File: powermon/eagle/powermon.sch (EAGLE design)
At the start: 25 parts, among them J1 USBSMD, J3 USBSMD, U1 LTC2290, U2 FT232RL, U3 ATMEGA328, X1 16MHz

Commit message: Updated schematic.
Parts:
- removed JP2: (no value), powermon:PINHD-1X2
- added C1, C4: 10uF, powermon:CPOL-USA/3216-18R
- added C5, C8, C9: 0.1uF, powermon:C-USC0805
- added J2: TERMINAL-2, powermon:TERMINAL-2
- added JP1: (no value), powermon:PINHD-1X9
- added R10: (no value), powermon:SHUNT
- added R11: 3.3K, powermon:R-US_R0805
- added R2: 8k 1%, powermon:R-US_R0805
- added R3: 3.3K 1%, powermon:R-US_R0805
- added R99: 1K, powermon:TRIM_US-SM-42/43A
- added S1: 219-04, powermon:219-04
- added U4: LTE1764, powermon:LTE1764
- U1: value LTC2290 -> INA219; device powermon:LTC2290 -> powermon:INA219
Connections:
- new net CONFIG1: S1.8, U3.PC3(ADC3)
- new net CONFIG2: S1.7, U3.PC2(ADC2)
- new net CONFIG3: S1.6, U3.PC1(ADC1)
- new net CONFIG4: S1.5, U3.PC0(ADC0)
- new net I2C-CLK: R11.1, U1.SCL, U3.PC5(ADC5/SCL)
- new net I2C-DATA: R1.1, U1.SDA, U3.PC4(ADC4/SDA)
- new net N$18: R3.1, R99.E, R99.S
- new net N$19: R2.2, R99.A, U4.ADJ
- new net N$5: J2.2, R10.I1, R2.1
- new net N$9: C4.+, C5.1, J1.VBUS, U4.IN, U4.SHDN
- new net SENSE+: R10.V2, U1.VIN+
- new net SENSE-: R10.V1, U1.VIN-
- new net V+: C1.+, C8.1, R10.I2, U4.OUT
- net +5V: now also C9.1, R1.2, R11.2
- net GND: now also C1.-, C4.-, C5.2, C8.2, C9.2, J1.GND, J2.1, R3.2, S1.1, S1.2, S1.3, S1.4, U4.GND@1, U4.GND@2
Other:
- note added: "FROM CHARGER"
- note added: "LOGIC ANALYZER"
- note added: "SETTINGS"
- note added: "TO COMPUTER"
- note added: "TO DEVICE"
- note added: "V/A SENSE"
- note added: "VOLTAGE REGULATOR"
- note removed: "POWER"
- note removed: "SENSE"
- moved on the sheet: C10, C2, C3, C6, C7, J1, J3, J5, R1, R4, U2, U3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

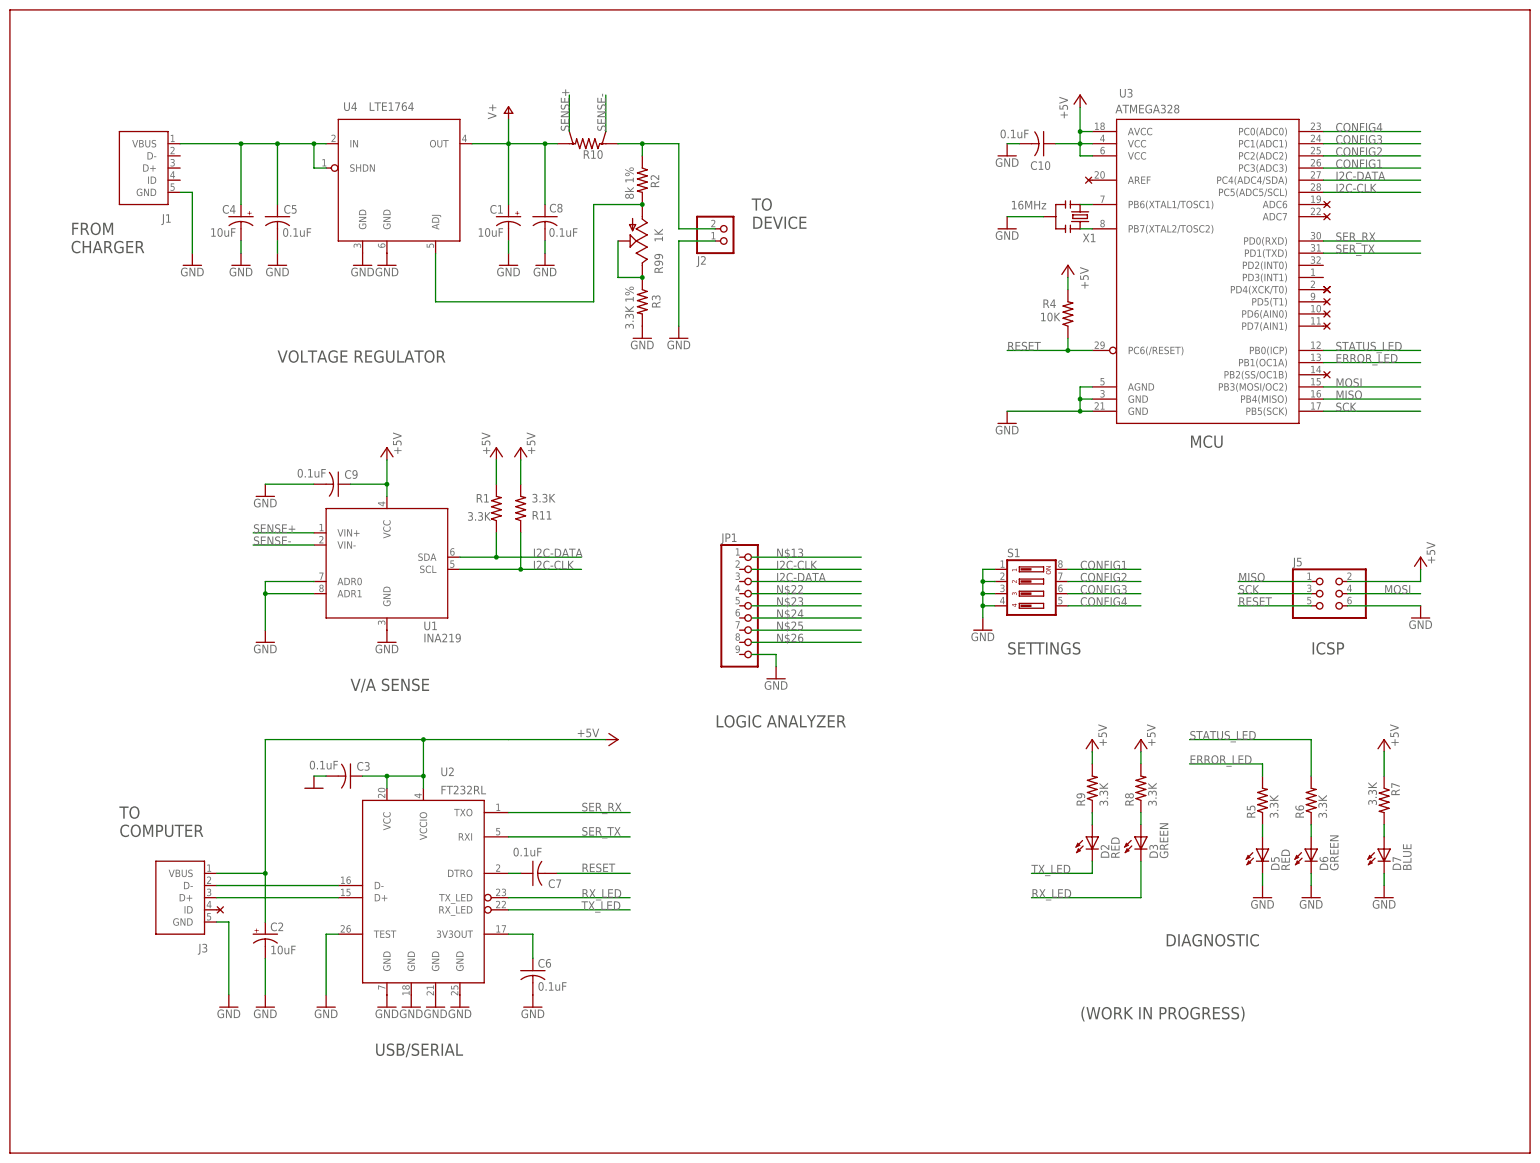
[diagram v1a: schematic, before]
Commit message: More progress with the powermon schematic. Incomplete.
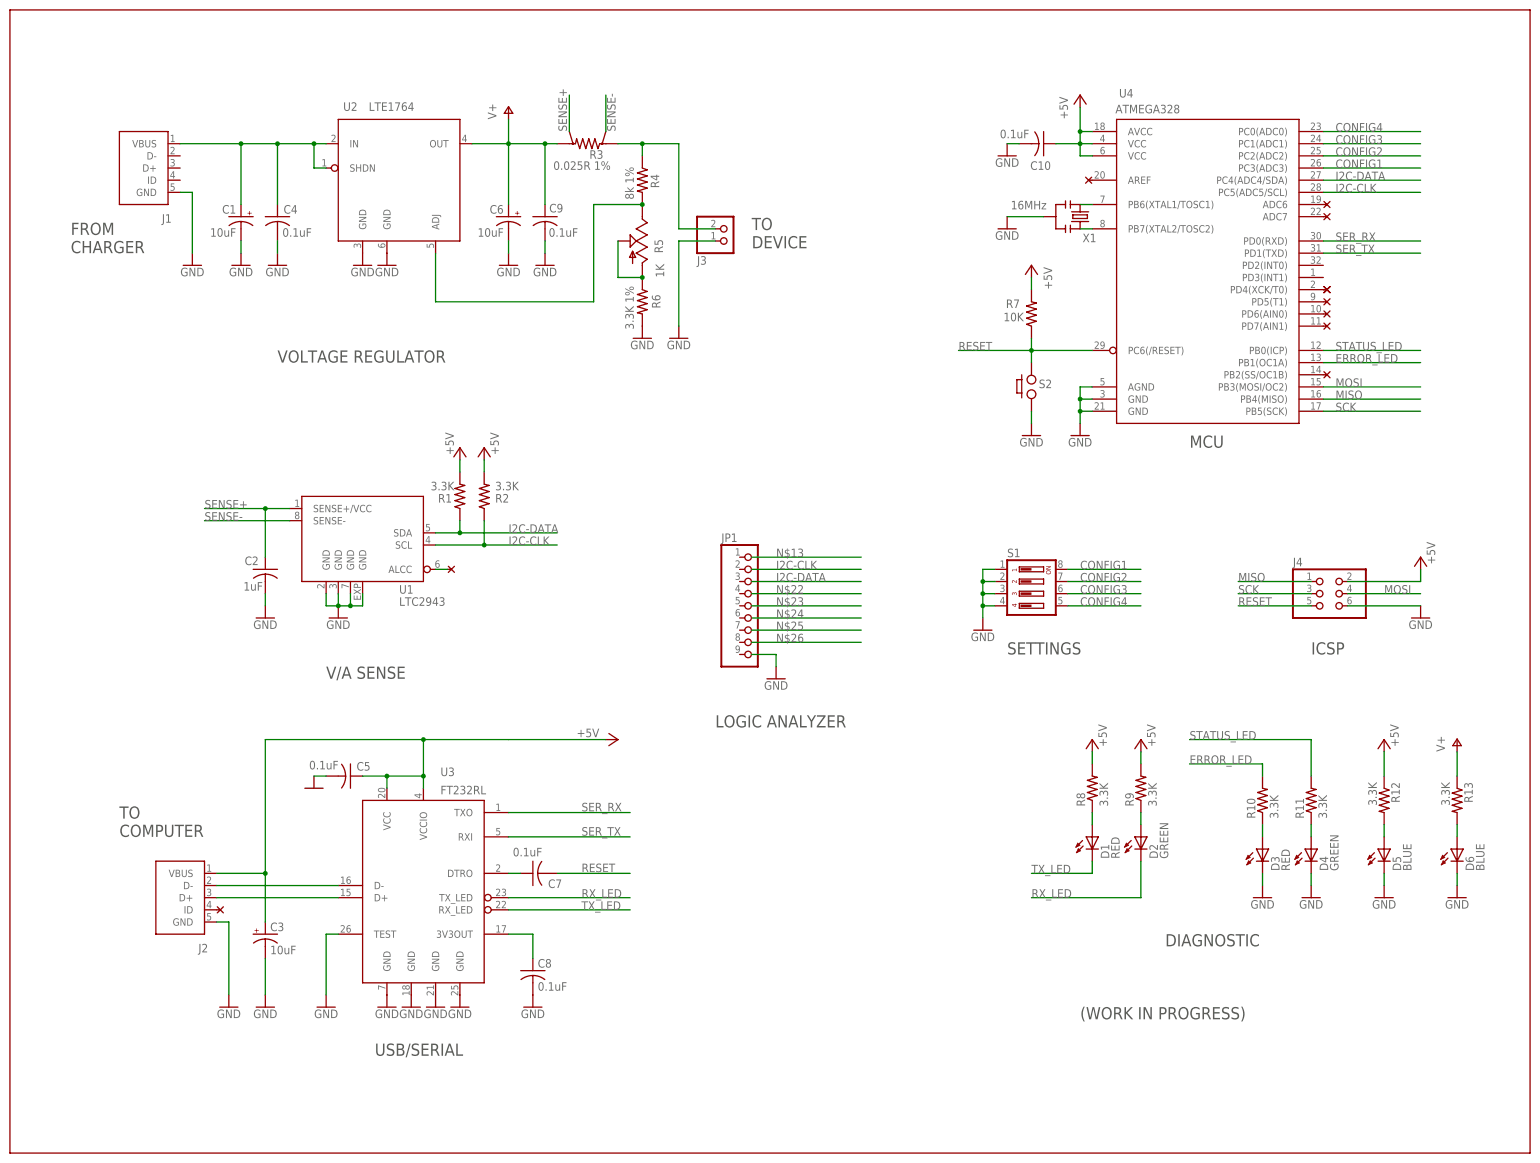
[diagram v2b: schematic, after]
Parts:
- removed D7: BLUE, powermon:LED
- removed R99: 1K, powermon:TRIM_US-SM-42/43A
- added D1: RED, powermon:LED
- added D4: GREEN, powermon:LED
- added R12, R13: 3.3K, powermon:R-US_R0805
- added S2: PUSH_BUTTON, powermon:PUSH_BUTTON
- C2: value 10uF -> 1uF; device powermon:CPOL-USA/3216-18R -> powermon:C-USC0805
- C3: value 0.1uF -> 10uF; device powermon:C-USC0805 -> powermon:CPOL-USA/3216-18R
- C4: value 10uF -> 0.1uF; device powermon:CPOL-USA/3216-18R -> powermon:C-USC0805
- C6: value 0.1uF -> 10uF; device analyzer:C-USC0805 -> powermon:CPOL-USA/3216-18R
- C8: device powermon:C-USC0805 -> analyzer:C-USC0805
- D2: value RED -> GREEN
- D3: value GREEN -> RED
- D5: value RED -> BLUE
- D6: value GREEN -> BLUE
- J2: value TERMINAL-2 -> USBSMD; device powermon:TERMINAL-2 -> powermon:USBSMD
- J3: value USBSMD -> TERMINAL-2; device powermon:USBSMD -> powermon:TERMINAL-2
- R10: value (none) -> 3.3K; device powermon:SHUNT -> powermon:R-US_R0805
- R2: value 8k 1% -> 3.3K
- R3: value 3.3K 1% -> 0.025R 1%; device powermon:R-US_R0805 -> powermon:SHUNT
- R4: value 10K -> 8k 1%
- R5: value 3.3K -> 1K; device powermon:R-US_R0805 -> powermon:TRIM_US-SM-42/43A
- R6: value 3.3K -> 3.3K 1%
- R7: value 3.3K -> 10K
- U1: value INA219 -> LTC2943; device powermon:INA219 -> powermon:LTC2943SMD
- U2: value FT232RL -> LTE1764; device powermon:FT232RL -> powermon:LTE1764
- U3: value ATMEGA328 -> FT232RL; device powermon:ATMEGA328 -> powermon:FT232RL
- U4: value LTE1764 -> ATMEGA328; device powermon:LTE1764 -> powermon:ATMEGA328
- renumbered J5 to J4
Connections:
- removed net N$8 (its old number): D3.A, R8.1
- new net GND@3: U1.GND@2, U1.GND@3, U1.GND@7, U1.GND@9
- new net N$1: U1.ALCC
- new net N$14: D6.A, R13.2
- new net N$6: D1.A, R8.1
- net +5V: now also R12.1, R2.2, R7.2, U4.AVCC, U4.VCC@1, U4.VCC@2; no longer C9.1, R11.2, R4.2, R7.1, U1.VCC, U3.AVCC, U3.VCC@1, U3.VCC@2
- net CONFIG1: now also U4.PC3(ADC3); no longer U3.PC3(ADC3)
- net CONFIG2: now also U4.PC2(ADC2); no longer U3.PC2(ADC2)
- net CONFIG3: now also U4.PC1(ADC1); no longer U3.PC1(ADC1)
- net CONFIG4: now also U4.PC0(ADC0); no longer U3.PC0(ADC0)
- net ERROR_LED: now also R10.2, U4.PB1(OC1A); no longer R5.2, U3.PB1(OC1A)
- net GND: now also C2.2, C3.-, C4.2, C6.-, D3.C, D4.C, J2.GND, J3.1, R6.2, S2.P$4, U3.GND@3, U3.GND@4, U3.TEST, U4.AGND; no longer C2.-, C3.2, C4.-, C6.2, D7.C, J2.1, J3.GND, R3.2, U1.ADR0, U1.ADR1, U1.GND, U2.GND@3, U2.GND@4, U2.TEST, U3.AGND
- net I2C-CLK: now also R2.1, U4.PC5(ADC5/SCL); no longer R11.1, U3.PC5(ADC5/SCL)
- net I2C-DATA: now also U4.PC4(ADC4/SDA); no longer U3.PC4(ADC4/SDA)
- net MISO: now also U4.PB4(MISO); no longer U3.PB4(MISO)
- net MOSI: now also U4.PB3(MOSI/OC2); no longer U3.PB3(MOSI/OC2)
- net N$10: now also J2.D+, U3.D+; no longer J3.D+, U2.D+
- net N$11: now also U3.DTRO; no longer U2.DTRO
- net N$12: now also C3.+, C5.1, J2.VBUS, U3.VCC, U3.VCCIO; no longer C2.+, C3.1, J3.VBUS, U2.VCC, U2.VCCIO
- net N$15: now also J2.D-, U3.D-; no longer J3.D-, U2.D-
- net N$16: now also C8.1, U3.3V3OUT; no longer C6.1, U2.3V3OUT
- net N$17: now also D5.A, R12.2; no longer D7.A, R7.2
- net N$18: now also R5.A, R5.S, R6.1; no longer R3.1, R99.E, R99.S
- net N$19: now also R4.2, R5.E, U2.ADJ; no longer R2.2, R99.A, U4.ADJ
- net N$2: now also U4.PB7(XTAL2/TOSC2); no longer U3.PB7(XTAL2/TOSC2)
- net N$3: now also D4.A, R11.1; no longer D6.A, R6.1
- net N$4: now also D3.A, R10.1; no longer D5.A, R5.1
- net N$5: now also J3.2, R3.I1, R4.1; no longer J2.2, R10.I1, R2.1
- net N$7: now also U4.PB6(XTAL1/TOSC1); no longer U3.PB6(XTAL1/TOSC1)
- net N$9: now also C1.+, C4.1, U2.IN, U2.SHDN; no longer C4.+, C5.1, U4.IN, U4.SHDN
- net RESET: now also R7.1, S2.P$3, U4.PC6(/RESET); no longer R4.1, U3.PC6(/RESET)
- net RX_LED: now also D2.C, U3.TX_LED; no longer D3.C, U2.TX_LED
- net SCK: now also U4.PB5(SCK); no longer U3.PB5(SCK)
- net SENSE+: now also C2.1, R3.V2, U1.SENSE+/VCC; no longer R10.V2, U1.VIN+
- net SENSE-: now also R3.V1, U1.SENSE-; no longer R10.V1, U1.VIN-
- net SER_RX: now also U3.TXO, U4.PD0(RXD); no longer U2.TXO, U3.PD0(RXD)
- net SER_TX: now also U3.RXI, U4.PD1(TXD); no longer U2.RXI, U3.PD1(TXD)
- net STATUS_LED: now also R11.2, U4.PB0(ICP); no longer R6.2, U3.PB0(ICP)
- net TX_LED: now also D1.C, U3.RX_LED; no longer D2.C, U2.RX_LED
- net V+: now also C6.+, C9.1, R13.1, R3.I2, U2.OUT; no longer C1.+, C8.1, R10.I2, U4.OUT
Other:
- moved on the sheet: C1, C5, C8, C9, D2, D3, D5, D6, R1, R11, R2, R4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

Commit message: Updated schematic.
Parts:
- U2: value LTE1764 -> LT1764AEQ
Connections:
- net STATUS_LED renamed ACTIVITY_LED
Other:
- note added: "3.8V"
- moved on the sheet: C1, C4, C6, C9, R7, S2
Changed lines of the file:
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@@
 <part name="P+7" library="powermon" deviceset="+5V" device=""/>
 <part name="GND4" library="powermon" deviceset="GND" device=""/>
-<part name="U2" library="powermon" deviceset="LTE1764" device=""/>
+<part name="U2" library="powermon" deviceset="LTE1764" device="" value="LT1764AEQ"/>
 <part name="GND19" library="powermon" deviceset="GND" device=""/>
 <part name="GND20" library="powermon" deviceset="GND" device=""/>
@@
 <text x="-22.86" y="187.96" size="2.54" layer="97">FROM
 CHARGER</text>
-<text x="111.76" y="88.9" size="2.54" layer="97">LOGIC ANALYZER</text>
+<text x="111.76" y="91.44" size="2.54" layer="97">LOGIC ANALYZER</text>
 <text x="-12.7" y="66.04" size="2.54" layer="97">TO
 COMPUTER</text>
@@
 DEVICE</text>
 <text x="172.72" y="104.14" size="2.54" layer="97">SETTINGS</text>
+<text x="97.028" y="213.106" size="2.54" layer="97">3.8V</text>
 </plain>
 <instances>
@@
 <attribute name="VALUE" x="173.482" y="198.882" size="1.778" layer="96" rot="MR180"/>
 </instance>
-<instance part="GND8" gate="1" x="172.72" y="193.04"/>
+<instance part="GND8" gate="1" x="170.18" y="193.04"/>
 <instance part="D3" gate="G$1" x="226.06" y="63.5"/>
 <instance part="D4" gate="G$1" x="236.22" y="63.5"/>
-<instance part="R7" gate="G$1" x="177.8" y="175.26" smashed="yes" rot="R90">
-<attribute name="NAME" x="172.466" y="176.5046" size="1.778" layer="95"/>
-<attribute name="VALUE" x="171.958" y="173.736" size="1.778" layer="96"/>
-</instance>
-<instance part="P+1" gate="1" x="177.8" y="185.42" rot="MR0"/>
+<instance part="R7" gate="G$1" x="180.34" y="175.26" smashed="yes" rot="R90">
+<attribute name="NAME" x="175.006" y="176.5046" size="1.778" layer="95"/>
+<attribute name="VALUE" x="174.498" y="173.736" size="1.778" layer="96"/>
+</instance>
+<instance part="P+1" gate="1" x="180.34" y="185.42" rot="MR0"/>
 <instance part="C10" gate="G$1" x="180.34" y="210.82" smashed="yes" rot="R270">
 <attribute name="NAME" x="177.546" y="205.359" size="1.778" layer="95"/>
@@
 </instance>
 <instance part="C3" gate="G$1" x="17.78" y="45.72"/>
-<instance part="GND1" gate="1" x="172.72" y="208.28" rot="MR0"/>
+<instance part="GND1" gate="1" x="170.18" y="208.28" rot="MR0"/>
 <instance part="D5" gate="G$1" x="251.46" y="63.5"/>
 <instance part="R12" gate="G$1" x="251.46" y="73.66" rot="R270"/>
@@
 <instance part="GND22" gate="1" x="96.52" y="170.18"/>
 <instance part="GND23" gate="1" x="104.14" y="170.18"/>
-<instance part="C6" gate="G$1" x="68.58" y="195.58" rot="MR0"/>
-<instance part="C1" gate="G$1" x="12.7" y="195.58" rot="MR0"/>
+<instance part="C6" gate="G$1" x="68.58" y="198.12" rot="MR0"/>
+<instance part="C1" gate="G$1" x="12.7" y="198.12" rot="MR0"/>
 <instance part="GND24" gate="1" x="12.7" y="185.42"/>
-<instance part="C4" gate="G$1" x="20.32" y="195.58" smashed="yes">
-<attribute name="NAME" x="21.59" y="196.215" size="1.778" layer="95"/>
-<attribute name="VALUE" x="21.336" y="191.389" size="1.778" layer="96"/>
+<instance part="C4" gate="G$1" x="20.32" y="198.12" smashed="yes">
+<attribute name="NAME" x="21.59" y="198.755" size="1.778" layer="95"/>
+<attribute name="VALUE" x="21.336" y="193.929" size="1.778" layer="96"/>
 </instance>
 <instance part="GND25" gate="1" x="20.32" y="185.42"/>
-<instance part="C9" gate="G$1" x="76.2" y="195.58" smashed="yes">
-<attribute name="NAME" x="80.01" y="198.247" size="1.778" layer="95" rot="R180"/>
-<attribute name="VALUE" x="76.962" y="191.389" size="1.778" layer="96"/>
+<instance part="C9" gate="G$1" x="76.2" y="198.12" smashed="yes">
+<attribute name="NAME" x="80.01" y="200.787" size="1.778" layer="95" rot="R180"/>
+<attribute name="VALUE" x="76.962" y="193.929" size="1.778" layer="96"/>
 </instance>
 <instance part="GND26" gate="1" x="68.58" y="185.42"/>
@@
 <instance part="GND28" gate="1" x="266.7" y="53.34" rot="MR0"/>
 <instance part="P+8" gate="1" x="266.7" y="86.36"/>
-<instance part="S2" gate="G$1" x="177.8" y="160.02"/>
-<instance part="GND31" gate="1" x="177.8" y="149.86"/>
+<instance part="S2" gate="G$1" x="180.34" y="160.02"/>
+<instance part="GND31" gate="1" x="180.34" y="149.86"/>
 </instances>
 <busses>
@@
 <segment>
 <pinref part="X1" gate="G$1" pin="2"/>
-<wire x1="180.34" y1="195.58" x2="172.72" y2="195.58" width="0.1524" layer="91"/>
+<wire x1="180.34" y1="195.58" x2="170.18" y2="195.58" width="0.1524" layer="91"/>
 <pinref part="GND8" gate="1" pin="GND"/>
 </segment>
@@
 <segment>
 <pinref part="C10" gate="G$1" pin="2"/>
-<wire x1="175.26" y1="210.82" x2="172.72" y2="210.82" width="0.1524" layer="91"/>
+<wire x1="175.26" y1="210.82" x2="170.18" y2="210.82" width="0.1524" layer="91"/>
 <pinref part="GND1" gate="1" pin="GND"/>
 </segment>
@@
 <pinref part="C1" gate="G$1" pin="-"/>
 <pinref part="GND24" gate="1" pin="GND"/>
-<wire x1="12.7" y1="190.5" x2="12.7" y2="187.96" width="0.1524" layer="91"/>
+<wire x1="12.7" y1="193.04" x2="12.7" y2="187.96" width="0.1524" layer="91"/>
 </segment>
 <segment>
 <pinref part="C4" gate="G$1" pin="2"/>
 <pinref part="GND25" gate="1" pin="GND"/>
-<wire x1="20.32" y1="190.5" x2="20.32" y2="187.96" width="0.1524" layer="91"/>
+<wire x1="20.32" y1="193.04" x2="20.32" y2="187.96" width="0.1524" layer="91"/>
 </segment>
 <segment>
 <pinref part="C6" gate="G$1" pin="-"/>
 <pinref part="GND26" gate="1" pin="GND"/>
-<wire x1="68.58" y1="190.5" x2="68.58" y2="187.96" width="0.1524" layer="91"/>
+<wire x1="68.58" y1="193.04" x2="68.58" y2="187.96" width="0.1524" layer="91"/>
 </segment>
 <segment>
 <pinref part="C9" gate="G$1" pin="2"/>
 <pinref part="GND27" gate="1" pin="GND"/>
-<wire x1="76.2" y1="190.5" x2="76.2" y2="187.96" width="0.1524" layer="91"/>
+<wire x1="76.2" y1="193.04" x2="76.2" y2="187.96" width="0.1524" layer="91"/>
 </segment>
 <segment>
@@
 <pinref part="S2" gate="G$1" pin="P$4"/>
 <pinref part="GND31" gate="1" pin="GND"/>
-<wire x1="177.8" y1="154.94" x2="177.8" y2="152.4" width="0.1524" layer="91"/>
+<wire x1="180.34" y1="154.94" x2="180.34" y2="152.4" width="0.1524" layer="91"/>
 </segment>
 </net>
@@
 <pinref part="P+1" gate="1" pin="+5V"/>
 <pinref part="R7" gate="G$1" pin="2"/>
-<wire x1="177.8" y1="182.88" x2="177.8" y2="180.34" width="0.1524" layer="91"/>
+<wire x1="180.34" y1="182.88" x2="180.34" y2="180.34" width="0.1524" layer="91"/>
 </segment>
 <segment>
@@
 <segment>
 <pinref part="U4" gate="G$1" pin="PC6(/RESET)"/>
-<wire x1="190.5" y1="167.64" x2="177.8" y2="167.64" width="0.1524" layer="91"/>
+<wire x1="190.5" y1="167.64" x2="180.34" y2="167.64" width="0.1524" layer="91"/>
 <pinref part="R7" gate="G$1" pin="1"/>
-<wire x1="177.8" y1="167.64" x2="162.56" y2="167.64" width="0.1524" layer="91"/>
-<wire x1="177.8" y1="170.18" x2="177.8" y2="167.64" width="0.1524" layer="91"/>
-<junction x="177.8" y="167.64"/>
-<label x="162.56" y="167.64" size="1.778" layer="95"/>
+<wire x1="180.34" y1="167.64" x2="167.64" y2="167.64" width="0.1524" layer="91"/>
+<wire x1="180.34" y1="170.18" x2="180.34" y2="167.64" width="0.1524" layer="91"/>
+<junction x="180.34" y="167.64"/>
+<label x="167.64" y="167.64" size="1.778" layer="95"/>
 <pinref part="S2" gate="G$1" pin="P$3"/>
-<wire x1="177.8" y1="165.1" x2="177.8" y2="167.64" width="0.1524" layer="91"/>
+<wire x1="180.34" y1="165.1" x2="180.34" y2="167.64" width="0.1524" layer="91"/>
 </segment>
 </net>
@@
 </segment>
 </net>
-<net name="STATUS_LED" class="0">
+<net name="ACTIVITY_LED" class="0">
 <segment>
 <wire x1="238.76" y1="167.64" x2="259.08" y2="167.64" width="0.1524" layer="91"/>
@@
 <wire x1="27.94" y1="205.74" x2="27.94" y2="210.82" width="0.1524" layer="91"/>
 <pinref part="C1" gate="G$1" pin="+"/>
-<wire x1="12.7" y1="198.12" x2="12.7" y2="210.82" width="0.1524" layer="91"/>
+<wire x1="12.7" y1="200.66" x2="12.7" y2="210.82" width="0.1524" layer="91"/>
 <pinref part="C4" gate="G$1" pin="1"/>
-<wire x1="20.32" y1="198.12" x2="20.32" y2="210.82" width="0.1524" layer="91"/>
+<wire x1="20.32" y1="200.66" x2="20.32" y2="210.82" width="0.1524" layer="91"/>
 <junction x="27.94" y="210.82"/>
 <junction x="20.32" y="210.82"/>
@@
 <wire x1="68.58" y1="210.82" x2="76.2" y2="210.82" width="0.4064" layer="91"/>
 <wire x1="76.2" y1="210.82" x2="78.74" y2="210.82" width="0.4064" layer="91"/>
-<wire x1="68.58" y1="198.12" x2="68.58" y2="210.82" width="0.1524" layer="91"/>
+<wire x1="68.58" y1="200.66" x2="68.58" y2="210.82" width="0.1524" layer="91"/>
 <pinref part="C9" gate="G$1" pin="1"/>
-<wire x1="76.2" y1="198.12" x2="76.2" y2="210.82" width="0.1524" layer="91"/>
+<wire x1="76.2" y1="200.66" x2="76.2" y2="210.82" width="0.1524" layer="91"/>
 <junction x="68.58" y="210.82"/>
 <junction x="76.2" y="210.82"/>
